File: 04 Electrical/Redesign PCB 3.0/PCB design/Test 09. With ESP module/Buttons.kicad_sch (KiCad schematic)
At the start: 10 parts, among them SW1 btn_home, SW2 btn_up, SW3 btn_down, SW4 btn_confirm, SW5 btn_back

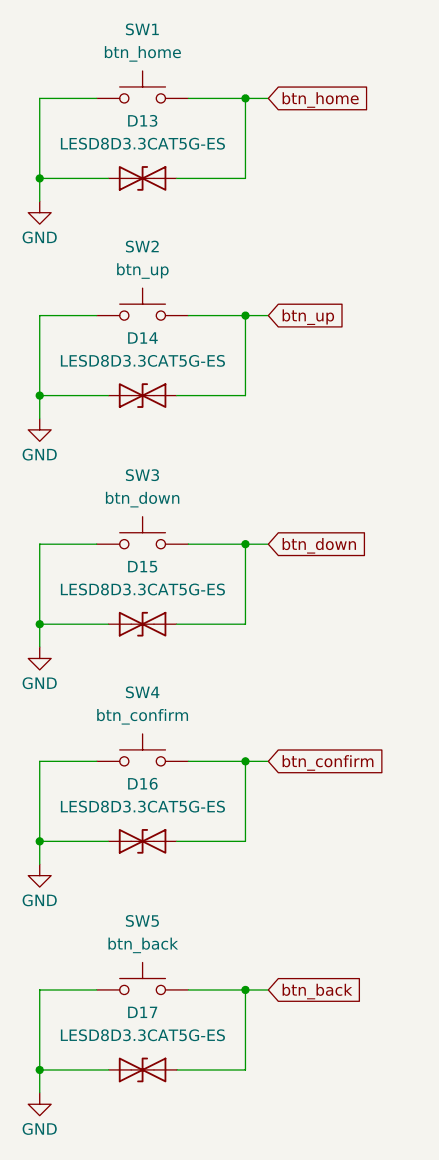
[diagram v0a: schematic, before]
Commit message: Logo added to PCB
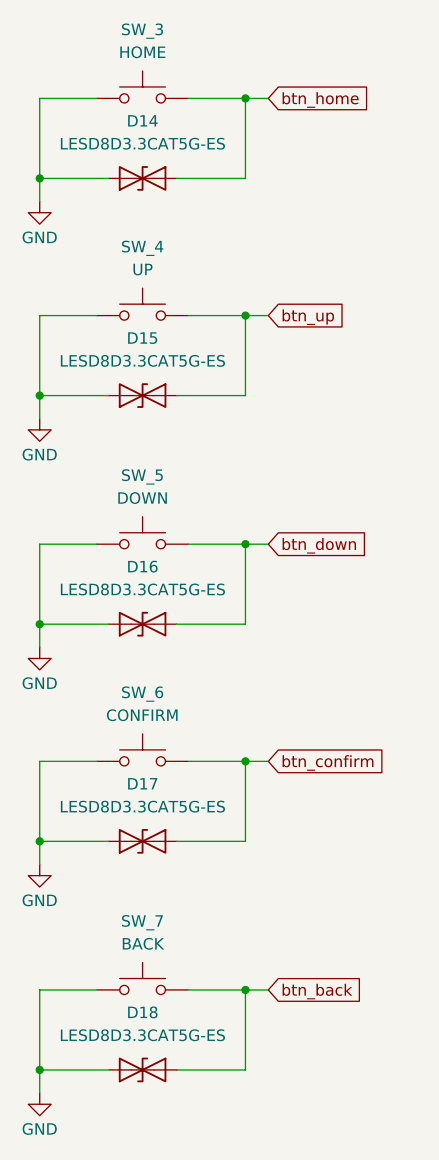
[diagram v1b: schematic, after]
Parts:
- removed SW1: btn_home, Project:SW_Push_SPEH, symbol Switch:SW_Push
- removed SW2: btn_up, Project:SW_Push_SPEH, symbol Switch:SW_Push
- removed SW3: btn_down, Project:SW_Push_SPEH, symbol Switch:SW_Push
- removed SW4: btn_confirm, Project:SW_Push_SPEH, symbol Switch:SW_Push
- removed SW5: btn_back, Project:SW_Push_SPEH, symbol Switch:SW_Push
- added SW_3: HOME, Button_Switch_SMD:SW_SPST_TL3342, symbol Switch:SW_Push
- added SW_4: UP, Button_Switch_SMD:SW_SPST_TL3342, symbol Switch:SW_Push
- added SW_5: DOWN, Button_Switch_SMD:SW_SPST_TL3342, symbol Switch:SW_Push
- added SW_6: CONFIRM, Button_Switch_SMD:SW_SPST_TL3342, symbol Switch:SW_Push
- added SW_7: BACK, Button_Switch_SMD:SW_SPST_TL3342, symbol Switch:SW_Push
- renumbered D13 to D14, D14 to D15, D15 to D16, D16 to D17, D17 to D18
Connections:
- net GND: now also SW_3.2, SW_4.2, SW_5.2, SW_6.2, SW_7.2
- net btn_back: now also SW_7.1
- net btn_confirm: now also SW_6.1
- net btn_down: now also SW_5.1
- net btn_home: now also SW_3.1
- net btn_up: now also SW_4.1

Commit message: As ordered at JLCPCB
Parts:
- SW_3, SW_4, SW_5, SW_6, SW_7: LCSC C318884 -> (none); LCSC Part #  (none) -> C318884
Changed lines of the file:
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@@
 		(on_board yes)
 		(dnp no)
-		(property "Reference" "#PWR031"
+		(property "Reference" "#PWR029"
 			(at 130.81 50.8 0)
 			(effects
@@
 			(project "Test 09. With ESP module"
 				(path "/dee7d3c3-6abb-4cb3-8df4-3e3e37989a04/c10dcd2b-f94d-4b79-ac64-852f0c201877"
-					(reference "#PWR031")
+					(reference "#PWR029")
 					(unit 1)
 				)
@@
 			)
 		)
-		(property "LCSC" "C318884"
+		(property "Comment" ""
+			(at 142.24 82.55 0)
+			(effects
+				(font
+					(size 1.27 1.27)
+				)
+				(hide yes)
+			)
+		)
+		(property "LCSC Part # " "C318884"
 			(at 142.24 82.55 0)
 			(effects
@@
 			)
 		)
-		(property "LCSC" "C318884"
+		(property "Comment" ""
+			(at 142.24 132.08 0)
+			(effects
+				(font
+					(size 1.27 1.27)
+				)
+				(hide yes)
+			)
+		)
+		(property "LCSC Part # " "C318884"
 			(at 142.24 132.08 0)
 			(effects
@@
 			)
 		)
-		(property "LCSC" "C318884"
+		(property "Comment" ""
+			(at 142.24 33.02 0)
+			(effects
+				(font
+					(size 1.27 1.27)
+				)
+				(hide yes)
+			)
+		)
+		(property "LCSC Part # " "C318884"
 			(at 142.24 33.02 0)
 			(effects
@@
 			)
 		)
+		(property "Comment" ""
+			(at 142.24 140.97 0)
+			(effects
+				(font
+					(size 1.27 1.27)
+				)
+				(hide yes)
+			)
+		)
 		(pin "2"
 		)
@@
 		(on_board yes)
 		(dnp no)
-		(property "Reference" "#PWR033"
+		(property "Reference" "#PWR031"
 			(at 130.81 100.33 0)
 			(effects
@@
 			(project "Test 09. With ESP module"
 				(path "/dee7d3c3-6abb-4cb3-8df4-3e3e37989a04/c10dcd2b-f94d-4b79-ac64-852f0c201877"
-					(reference "#PWR033")
+					(reference "#PWR031")
 					(unit 1)
 				)
@@
 			)
 		)
+		(property "Comment" ""
+			(at 142.24 115.57 0)
+			(effects
+				(font
+					(size 1.27 1.27)
+				)
+				(hide yes)
+			)
+		)
 		(pin "2"
 		)
@@
 			)
 		)
+		(property "Comment" ""
+			(at 142.24 91.44 0)
+			(effects
+				(font
+					(size 1.27 1.27)
+				)
+				(hide yes)
+			)
+		)
 		(pin "2"
 		)
@@
 			)
 		)
-		(property "LCSC" "C318884"
+		(property "Comment" ""
+			(at 142.24 106.68 0)
+			(effects
+				(font
+					(size 1.27 1.27)
+				)
+				(hide yes)
+			)
+		)
+		(property "LCSC Part # " "C318884"
 			(at 142.24 106.68 0)
 			(effects
@@
 		(on_board yes)
 		(dnp no)
-		(property "Reference" "#PWR034"
+		(property "Reference" "#PWR032"
 			(at 130.81 124.46 0)
 			(effects
@@
 			(project "Test 09. With ESP module"
 				(path "/dee7d3c3-6abb-4cb3-8df4-3e3e37989a04/c10dcd2b-f94d-4b79-ac64-852f0c201877"
-					(reference "#PWR034")
+					(reference "#PWR032")
 					(unit 1)
 				)
@@
 			)
 		)
+		(property "Comment" ""
+			(at 142.24 41.91 0)
+			(effects
+				(font
+					(size 1.27 1.27)
+				)
+				(hide yes)
+			)
+		)
 		(pin "2"
 		)
@@
 			)
 		)
-		(property "LCSC" "C318884"
+		(property "Comment" ""
+			(at 142.24 57.15 0)
+			(effects
+				(font
+					(size 1.27 1.27)
+				)
+				(hide yes)
+			)
+		)
+		(property "LCSC Part # " "C318884"
 			(at 142.24 57.15 0)
 			(effects
@@
 		(on_board yes)
 		(dnp no)
-		(property "Reference" "#PWR032"
+		(property "Reference" "#PWR030"
 			(at 130.81 74.93 0)
 			(effects
@@
 			(project "Test 09. With ESP module"
 				(path "/dee7d3c3-6abb-4cb3-8df4-3e3e37989a04/c10dcd2b-f94d-4b79-ac64-852f0c201877"
-					(reference "#PWR032")
+					(reference "#PWR030")
 					(unit 1)
 				)
@@
 			)
 		)
+		(property "Comment" ""
+			(at 142.24 66.04 0)
+			(effects
+				(font
+					(size 1.27 1.27)
+				)
+				(hide yes)
+			)
+		)
 		(pin "2"
 		)
@@
 		(on_board yes)
 		(dnp no)
-		(property "Reference" "#PWR035"
+		(property "Reference" "#PWR033"
 			(at 130.81 149.86 0)
 			(effects
@@
 			(project "Test 09. With ESP module"
 				(path "/dee7d3c3-6abb-4cb3-8df4-3e3e37989a04/c10dcd2b-f94d-4b79-ac64-852f0c201877"
-					(reference "#PWR035")
-					(unit 1)
-				)
+					(reference "#PWR033")
+					(unit 1)
+				)
